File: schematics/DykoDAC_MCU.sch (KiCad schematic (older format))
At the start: 38 parts, among them J3 USB_B, J4 OLED, J5 Debug, J6 Conn_01x05, J7 Conn_01x04, J8 Conn_01x05, J9 Conn_01x04, SW1 PEC09-2120K, U11 PRTR5V0U2X.215, U13 ATSAMD51J20A-A

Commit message: pcb
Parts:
- J4: footprint Pin_Headers:Pin_Header_Angled_1x04_Pitch2.54mm -> Pin_Headers:Pin_Header_Straight_1x04_Pitch2.54mm
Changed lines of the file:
@@
 F 0 "J4" H 2430 4842 50  0000 L CNN
 F 1 "OLED" H 2430 4751 50  0000 L CNN
-F 2 "Pin_Headers:Pin_Header_Angled_1x04_Pitch2.54mm" H 2350 4850 50  0001 C CNN
+F 2 "Pin_Headers:Pin_Header_Straight_1x04_Pitch2.54mm" H 2350 4850 50  0001 C CNN
 F 3 "~" H 2350 4850 50  0001 C CNN
 	1    2350 4850

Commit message: minor chages
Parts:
- added C51, C69: 10u, Capacitor_Tantalum_SMD:CP_EIA-3216-18_Kemet-A, symbol Device:CP
- U11: symbol kamtar:PRTR5V0U2X.215 -> DykoDAC-rescue:PRTR5V0U2X.215-kamtar
- U13: symbol MCU_Microchip_SAMD:ATSAMD51J20A-A -> DykoDAC-rescue:ATSAMD51J20A-A-MCU_Microchip_SAMD
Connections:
- wire segments 173 -> 179
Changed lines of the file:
@@
 	1900 1250 2550 1250
 $Comp
-L kamtar:PRTR5V0U2X.215 U11
+L DykoDAC-rescue:PRTR5V0U2X.215-kamtar U11
 U 1 1 5D1D054C
 P 2300 2200
+AR Path="/5D1D054C" Ref="U11"  Part="1"
+AR Path="/5CF60BAD/5D1D054C" Ref="U11"  Part="1"
 F 0 "U11" H 2678 2302 47  0000 L CNN
 F 1 "PRTR5V0U2X.215" H 2678 2215 47  0000 L CNN
@@
 $EndComp
 Wire Wire Line
-	4600 2250 4950 2250
+	4600 2250 4800 2250
 Wire Wire Line
 	4950 2350 4450 2350
@@
 	1650 5050 2150 5050
 $Comp
-L MCU_Microchip_SAMD:ATSAMD51J20A-A U13
+L DykoDAC-rescue:ATSAMD51J20A-A-MCU_Microchip_SAMD U13
 U 1 1 5E56127F
 P 8700 3350
+AR Path="/5E56127F" Ref="U13"  Part="1"
+AR Path="/5CF60BAD/5E56127F" Ref="U13"  Part="1"
 F 0 "U13" H 8700 3450 50  0000 C CNN
 F 1 "ATSAMD51J20A-A" H 8700 3300 50  0000 C CNN
@@
 Wire Wire Line
 	7200 4650 8000 4650
+$Comp
+L Device:CP C51
+U 1 1 5E63EAFA
+P 1500 4000
+F 0 "C51" V 1245 4000 50  0000 C CNN
+F 1 "10u" V 1336 4000 50  0000 C CNN
+F 2 "Capacitor_Tantalum_SMD:CP_EIA-3216-18_Kemet-A" H 1538 3850 50  0001 C CNN
+F 3 "~" H 1500 4000 50  0001 C CNN
+	1    1500 4000
+	0    1    1    0
+$EndComp
+Wire Wire Line
+	1650 4000 1950 4000
+Connection ~ 1950 4000
+$Comp
+L power:GND #PWR0101
+U 1 1 5E6490E5
+P 1250 4100
+F 0 "#PWR0101" H 1250 3850 50  0001 C CNN
+F 1 "GND" H 1255 3927 50  0000 C CNN
+F 2 "" H 1250 4100 50  0001 C CNN
+F 3 "" H 1250 4100 50  0001 C CNN
+	1    1250 4100
+	1    0    0    -1
+$EndComp
+Wire Wire Line
+	1250 4100 1250 4000
+Wire Wire Line
+	1250 4000 1350 4000
+$Comp
+L Device:CP C69
+U 1 1 5E652CBF
+P 4800 2000
+F 0 "C69" H 4682 1954 50  0000 R CNN
+F 1 "10u" H 4682 2045 50  0000 R CNN
+F 2 "Capacitor_Tantalum_SMD:CP_EIA-3216-18_Kemet-A" H 4838 1850 50  0001 C CNN
+F 3 "~" H 4800 2000 50  0001 C CNN
+	1    4800 2000
+	-1   0    0    1
+$EndComp
+$Comp
+L power:GND #PWR0102
+U 1 1 5E653C87
+P 4800 1700
+F 0 "#PWR0102" H 4800 1450 50  0001 C CNN
+F 1 "GND" H 4805 1527 50  0000 C CNN
+F 2 "" H 4800 1700 50  0001 C CNN
+F 3 "" H 4800 1700 50  0001 C CNN
+	1    4800 1700
+	-1   0    0    1
+$EndComp
+Wire Wire Line
+	4800 1850 4800 1700
+Wire Wire Line
+	4800 2150 4800 2250
+Connection ~ 4800 2250
+Wire Wire Line
+	4800 2250 4950 2250
 $EndSCHEMATC

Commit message: first revision finished
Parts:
- added SW2: Button A, Button_Switch_THT:SW_Tactile_SPST_Angled_PTS645Vx58-2LFS, symbol Switch:SW_Push
- added SW3: Button B, Button_Switch_THT:SW_Tactile_SPST_Angled_PTS645Vx58-2LFS, symbol Switch:SW_Push
- added SW4: The Button, Button_Switch_THT:SW_Tactile_SPST_Angled_PTS645Vx58-2LFS, symbol Switch:SW_Push
- SW1: value PEC09-2120K -> EC11B152420G; footprint Potentiometers:Potentiometer_Alps_RK097_Double_Vertical -> kamtar:Potentiometer_Alps_RK097_Dual_Horizontal
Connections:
- net +3V3: no longer C69.1
- net 3V3_Conn: now also C69.1
- net BTT: now also SW4.1
- net GND: now also SW2.2, SW3.2, SW4.2
- net BA: now reaches C56.2, J8.2 (Pin_2), R28.2, SW1.A
- net BA: now also SW2.1
- net BB: now reaches C57.1, J8.3 (Pin_3), R29.1, SW1.B
- net BB: now also SW3.1
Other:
- moved on the sheet: C56, C57, C58, C66, C69, D3, J5, R28, R29, R30, R38, R39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

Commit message: update
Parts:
- C59: footprint Capacitors_Tantalum_SMD:CP_Tantalum_Case-A_EIA-3216-18_Reflow -> Capacitor_Tantalum_SMD:CP_EIA-3216-18_Kemet-A
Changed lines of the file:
@@
 F 0 "C59" V 8950 1100 50  0000 C CNN
 F 1 "10u" V 8850 1100 50  0000 C CNN
-F 2 "Capacitors_Tantalum_SMD:CP_Tantalum_Case-A_EIA-3216-18_Reflow" H 8938 1100 50  0001 C CNN
+F 2 "Capacitor_Tantalum_SMD:CP_EIA-3216-18_Kemet-A" H 8938 1100 50  0001 C CNN
 F 3 "~" H 8900 1250 50  0001 C CNN
 	1    8900 1250

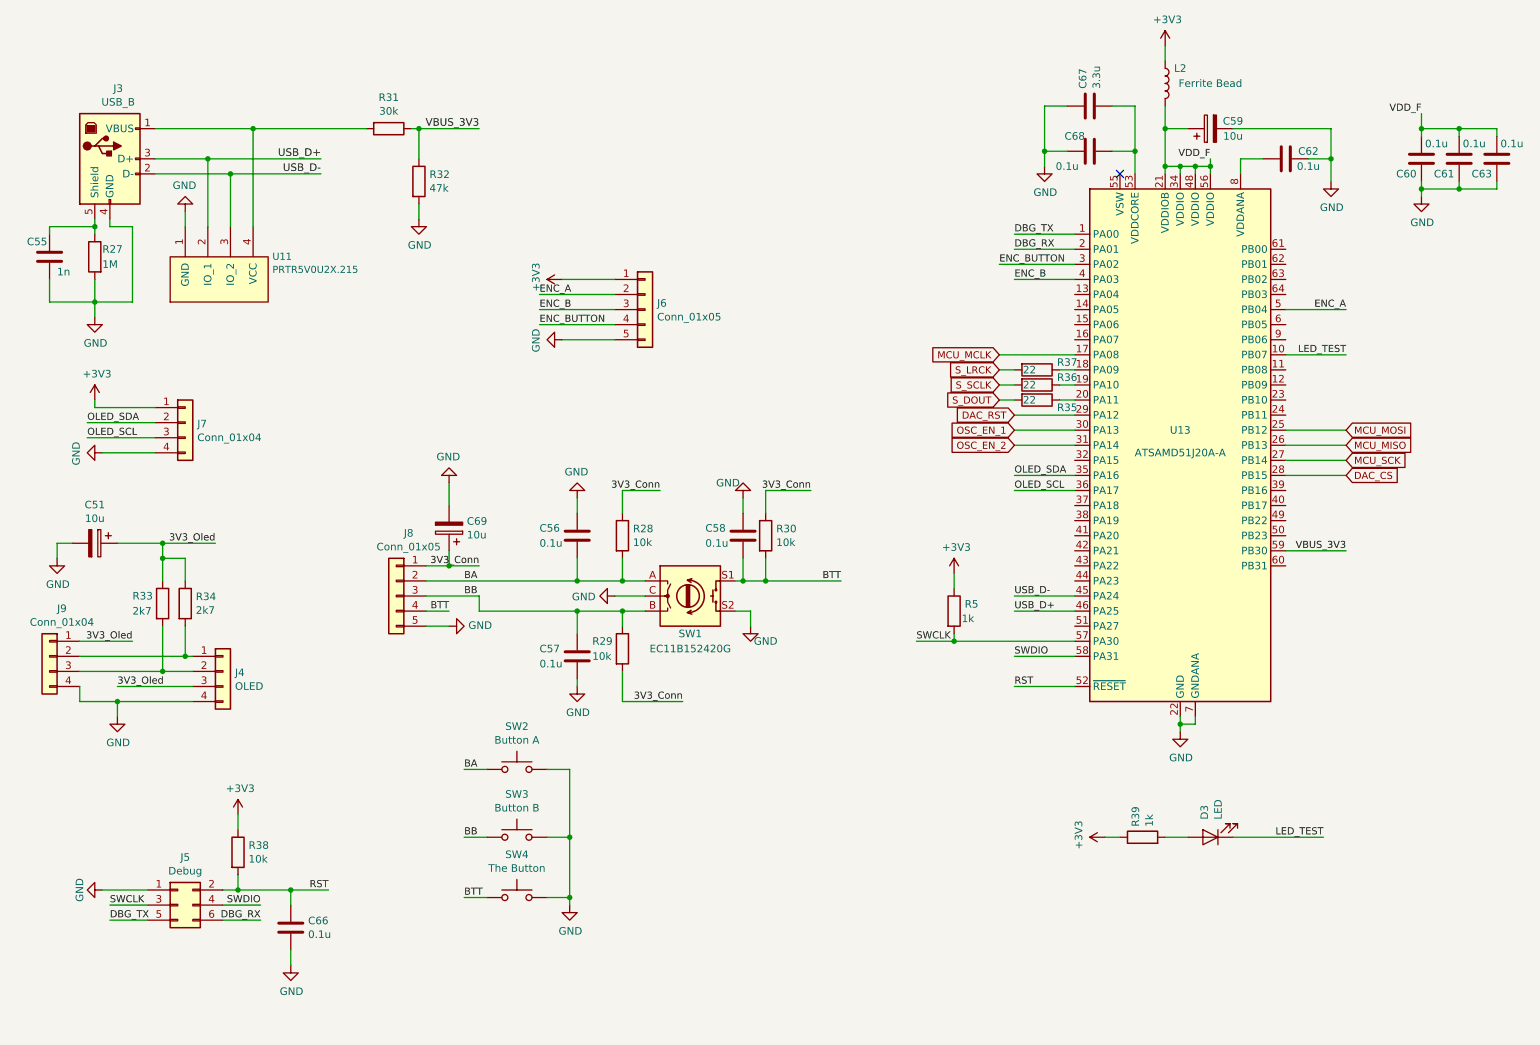
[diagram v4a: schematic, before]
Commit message: 9V -> 12V symbol
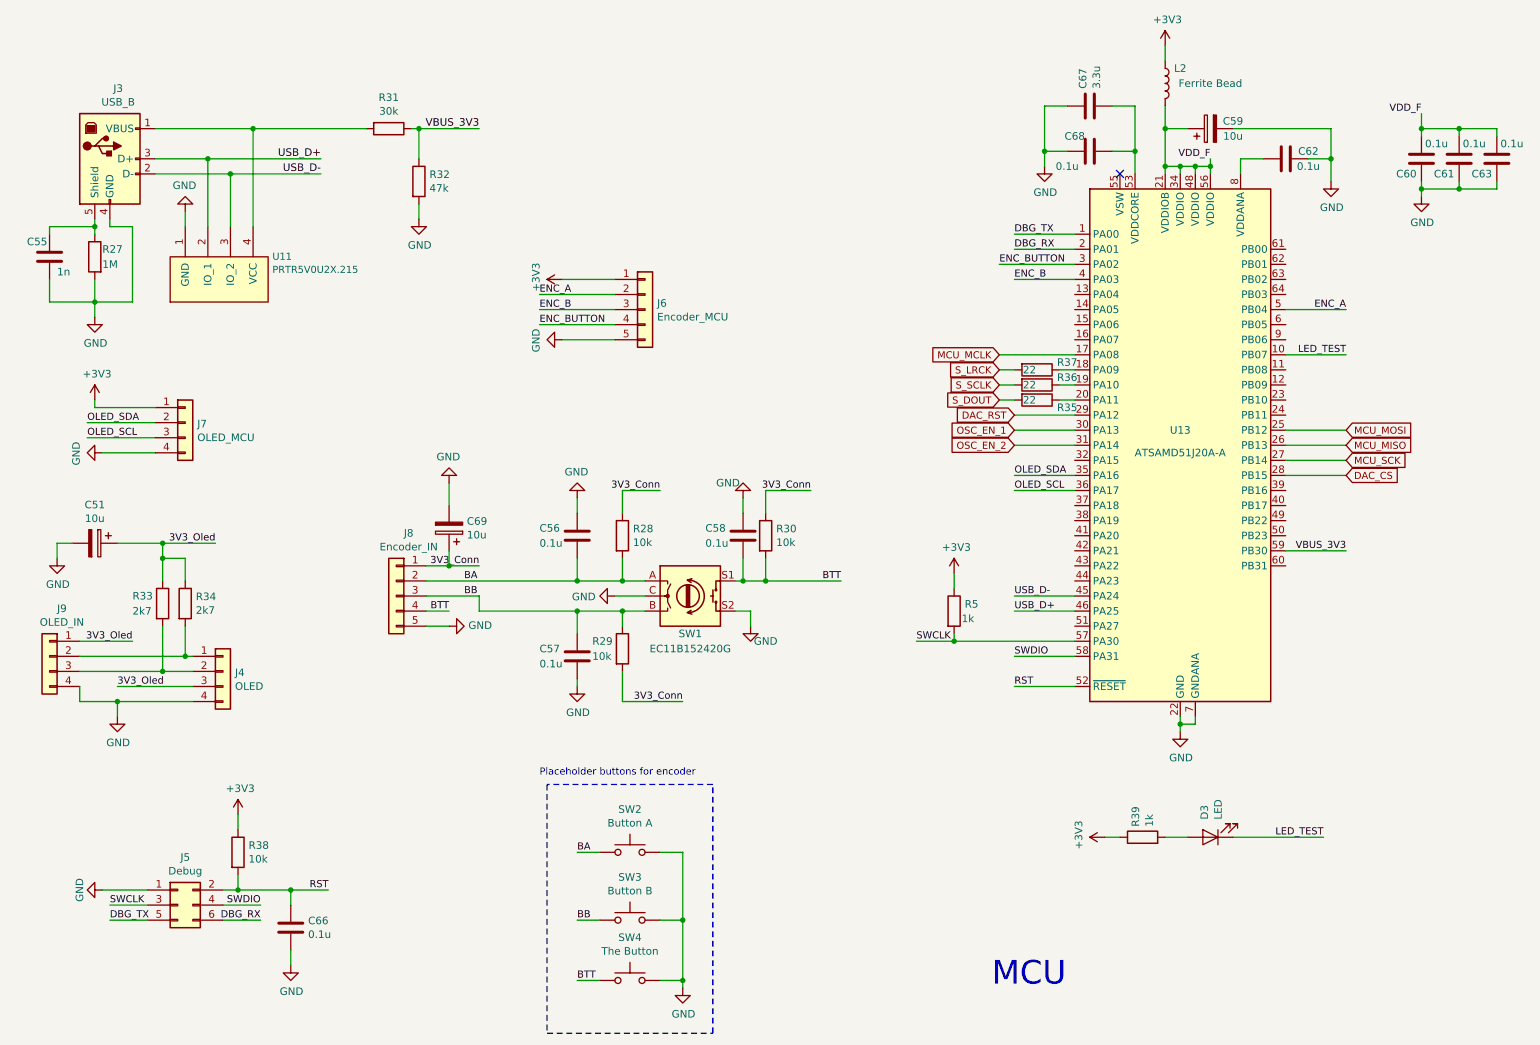
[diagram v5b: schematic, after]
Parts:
- J6: value Conn_01x05 -> Encoder_MCU
- J7: value Conn_01x04 -> OLED_MCU
- J8: value Conn_01x05 -> Encoder_IN
- J9: value Conn_01x04 -> OLED_IN
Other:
- note added: "MCU"
- note added: "Placeholder buttons for encoder"
- moved on the sheet: SW2, SW3, SW4
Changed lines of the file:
@@
 P 5150 2450
 F 0 "J6" H 5230 2492 50  0000 L CNN
-F 1 "Conn_01x05" H 5230 2401 50  0000 L CNN
+F 1 "Encoder_MCU" H 5230 2401 50  0000 L CNN
 F 2 "Pin_Headers:Pin_Header_Straight_1x05_Pitch2.00mm" H 5150 2450 50  0001 C CNN
 F 3 "~" H 5150 2450 50  0001 C CNN
@@
 P 3500 4350
 F 0 "J8" H 3418 4767 50  0000 C CNN
-F 1 "Conn_01x05" H 3418 4676 50  0000 C CNN
+F 1 "Encoder_IN" H 3418 4676 50  0000 C CNN
 F 2 "Pin_Headers:Pin_Header_Straight_1x05_Pitch2.00mm" H 3500 4350 50  0001 C CNN
 F 3 "~" H 3500 4350 50  0001 C CNN
@@
 P 2100 3200
 F 0 "J7" H 2180 3192 50  0000 L CNN
-F 1 "Conn_01x04" H 2180 3101 50  0000 L CNN
+F 1 "OLED_MCU" H 2180 3101 50  0000 L CNN
 F 2 "Pin_Headers:Pin_Header_Straight_1x04_Pitch2.00mm" H 2100 3200 50  0001 C CNN
 F 3 "~" H 2100 3200 50  0001 C CNN
@@
 P 1200 4750
 F 0 "J9" H 1118 5067 50  0000 C CNN
-F 1 "Conn_01x04" H 1118 4976 50  0000 C CNN
+F 1 "OLED_IN" H 1118 4976 50  0000 C CNN
 F 2 "Pin_Headers:Pin_Header_Straight_1x04_Pitch2.00mm" H 1200 4750 50  0001 C CNN
 F 3 "~" H 1200 4750 50  0001 C CNN
@@
 L Switch:SW_Push SW2
 U 1 1 5E69B240
-P 4300 5500
-F 0 "SW2" H 4300 5785 50  0000 C CNN
-F 1 "Button A" H 4300 5694 50  0000 C CNN
-F 2 "Button_Switch_THT:SW_Tactile_SPST_Angled_PTS645Vx58-2LFS" H 4300 5700 50  0001 C CNN
-F 3 "~" H 4300 5700 50  0001 C CNN
-	1    4300 5500
+P 5050 6050
+F 0 "SW2" H 5050 6335 50  0000 C CNN
+F 1 "Button A" H 5050 6244 50  0000 C CNN
+F 2 "Button_Switch_THT:SW_Tactile_SPST_Angled_PTS645Vx58-2LFS" H 5050 6250 50  0001 C CNN
+F 3 "~" H 5050 6250 50  0001 C CNN
+	1    5050 6050
 	1    0    0    -1
 $EndComp
@@
 L Switch:SW_Push SW3
 U 1 1 5E69D089
-P 4300 5950
-F 0 "SW3" H 4300 6235 50  0000 C CNN
-F 1 "Button B" H 4300 6144 50  0000 C CNN
-F 2 "Button_Switch_THT:SW_Tactile_SPST_Angled_PTS645Vx58-2LFS" H 4300 6150 50  0001 C CNN
-F 3 "~" H 4300 6150 50  0001 C CNN
-	1    4300 5950
+P 5050 6500
+F 0 "SW3" H 5050 6785 50  0000 C CNN
+F 1 "Button B" H 5050 6694 50  0000 C CNN
+F 2 "Button_Switch_THT:SW_Tactile_SPST_Angled_PTS645Vx58-2LFS" H 5050 6700 50  0001 C CNN
+F 3 "~" H 5050 6700 50  0001 C CNN
+	1    5050 6500
 	1    0    0    -1
 $EndComp
@@
 L Switch:SW_Push SW4
 U 1 1 5E69D7E1
-P 4300 6350
-F 0 "SW4" H 4300 6635 50  0000 C CNN
-F 1 "The Button" H 4300 6544 50  0000 C CNN
-F 2 "Button_Switch_THT:SW_Tactile_SPST_Angled_PTS645Vx58-2LFS" H 4300 6550 50  0001 C CNN
-F 3 "~" H 4300 6550 50  0001 C CNN
-	1    4300 6350
-	1    0    0    -1
-$EndComp
-Text Label 3950 5500 0    47   ~ 0
+P 5050 6900
+F 0 "SW4" H 5050 7185 50  0000 C CNN
+F 1 "The Button" H 5050 7094 50  0000 C CNN
+F 2 "Button_Switch_THT:SW_Tactile_SPST_Angled_PTS645Vx58-2LFS" H 5050 7100 50  0001 C CNN
+F 3 "~" H 5050 7100 50  0001 C CNN
+	1    5050 6900
+	1    0    0    -1
+$EndComp
+Text Label 4700 6050 0    47   ~ 0
 BA
-Text Label 3950 5950 0    47   ~ 0
+Text Label 4700 6500 0    47   ~ 0
 BB
-Text Label 3950 6350 0    47   ~ 0
+Text Label 4700 6900 0    47   ~ 0
 BTT
 Wire Wire Line
-	4100 6350 3950 6350
-Wire Wire Line
-	4100 5950 3950 5950
-Wire Wire Line
-	4100 5500 3950 5500
-Wire Wire Line
-	4500 5500 4650 5500
-Wire Wire Line
-	4650 5500 4650 5950
+	4850 6900 4700 6900
+Wire Wire Line
+	4850 6500 4700 6500
+Wire Wire Line
+	4850 6050 4700 6050
+Wire Wire Line
+	5250 6050 5400 6050
+Wire Wire Line
+	5400 6050 5400 6500
 $Comp
 L power:GND #PWR063
 U 1 1 5E6C4F87
-P 4650 6400
-F 0 "#PWR063" H 4650 6150 50  0001 C CNN
-F 1 "GND" H 4655 6227 50  0000 C CNN
-F 2 "" H 4650 6400 50  0001 C CNN
-F 3 "" H 4650 6400 50  0001 C CNN
-	1    4650 6400
-	1    0    0    -1
-$EndComp
-Wire Wire Line
-	4500 5950 4650 5950
-Connection ~ 4650 5950
-Wire Wire Line
-	4650 5950 4650 6350
-Wire Wire Line
-	4500 6350 4650 6350
-Connection ~ 4650 6350
-Wire Wire Line
-	4650 6350 4650 6400
+P 5400 6950
+F 0 "#PWR063" H 5400 6700 50  0001 C CNN
+F 1 "GND" H 5405 6777 50  0000 C CNN
+F 2 "" H 5400 6950 50  0001 C CNN
+F 3 "" H 5400 6950 50  0001 C CNN
+	1    5400 6950
+	1    0    0    -1
+$EndComp
+Wire Wire Line
+	5250 6500 5400 6500
+Connection ~ 5400 6500
+Wire Wire Line
+	5400 6500 5400 6900
+Wire Wire Line
+	5250 6900 5400 6900
+Connection ~ 5400 6900
+Wire Wire Line
+	5400 6900 5400 6950
 Connection ~ 3850 4150
 Wire Wire Line
@@
 Wire Wire Line
 	4600 2250 4950 2250
+Text Notes 7450 6950 0    157  ~ 0
+MCU
+Wire Notes Line
+	4500 5600 4500 7250
+Wire Notes Line
+	4500 7250 5600 7250
+Wire Notes Line
+	5600 7250 5600 5600
+Wire Notes Line
+	5600 5600 4500 5600
+Text Notes 4450 5550 0    47   ~ 0
+Placeholder buttons for encoder
 $EndSCHEMATC

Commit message: minor changes & pdf update
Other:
- moved on the sheet: C56, C57, C58, C69, J8, R28, R29, R30, R5, SW1

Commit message: cosmetic changes
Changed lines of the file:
@@
 P 7750 2950
 F 0 "R36" V 7700 3150 50  0000 C CNN
-F 1 "22" V 7750 2900 50  0000 C CNN
+F 1 "22" V 7750 2950 50  0000 C CNN
 F 2 "Resistors_SMD:R_0603" V 7680 2950 50  0001 C CNN
 F 3 "~" H 7750 2950 50  0001 C CNN
@@
 P 7750 2850
 F 0 "R37" V 7700 3050 50  0000 C CNN
-F 1 "22" V 7750 2800 50  0000 C CNN
+F 1 "22" V 7750 2850 50  0000 C CNN
 F 2 "Resistors_SMD:R_0603" V 7680 2850 50  0001 C CNN
 F 3 "~" H 7750 2850 50  0001 C CNN
@@
 P 7750 3050
 F 0 "R35" V 7800 3250 50  0000 C CNN
-F 1 "22" V 7750 3000 50  0000 C CNN
+F 1 "22" V 7750 3050 50  0000 C CNN
 F 2 "Resistors_SMD:R_0603" V 7680 3050 50  0001 C CNN
 F 3 "~" H 7750 3050 50  0001 C CNN
